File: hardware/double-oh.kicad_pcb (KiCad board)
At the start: 2 copper layers, 81.6 x 14 mm, 49 parts, among them J1 USB_B_Micro, J10 Conn_01x01, J11 Conn_01x01, J12 Conn_01x01, J13 Conn_01x01, J2 Conn_01x01, J3 Conn_01x01, J4 Conn_01x01, J5 Conn_01x01, J6 Conn_01x01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

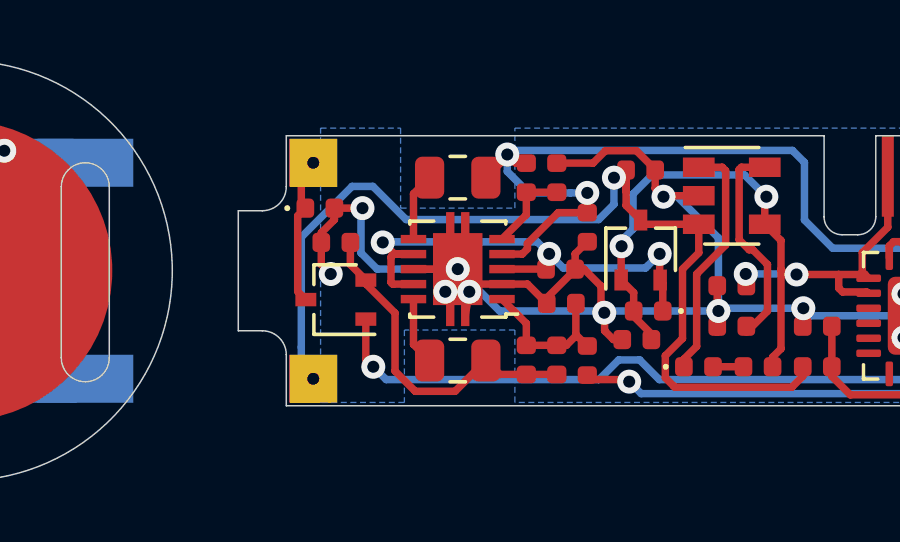
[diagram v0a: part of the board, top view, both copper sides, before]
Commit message: Rerouted for more thermal vias under buck converter
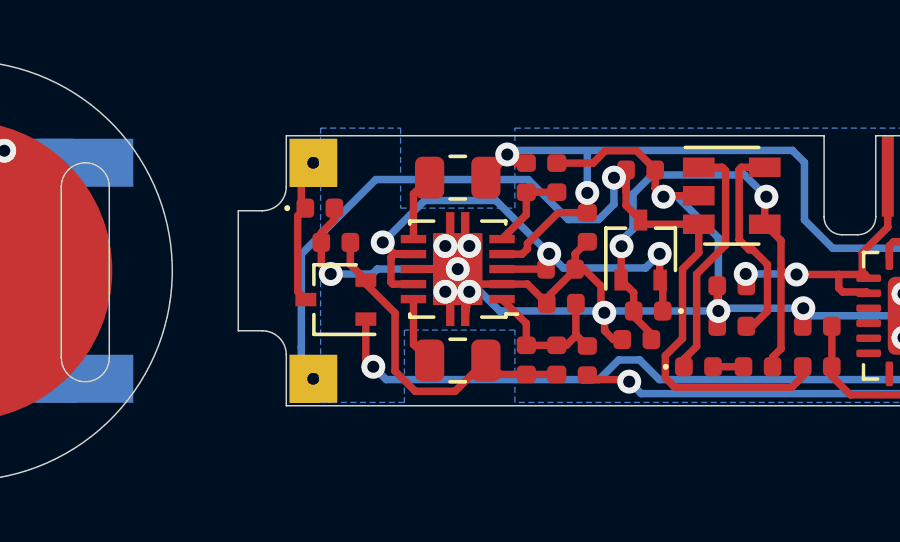
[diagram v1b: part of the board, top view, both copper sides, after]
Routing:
- net 3.3V: track 59.7 -> 57.5 mm
- net 0V: track 98.2 -> 96.6 mm, vias 25 -> 26
- net Net-(C11-Pad1): track 17.4 -> 18.5 mm

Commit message: Update DAC pin for battery level control
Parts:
- R12: value 330kΩ -> 300kΩ
- R9: value 480kΩ -> 470kΩ

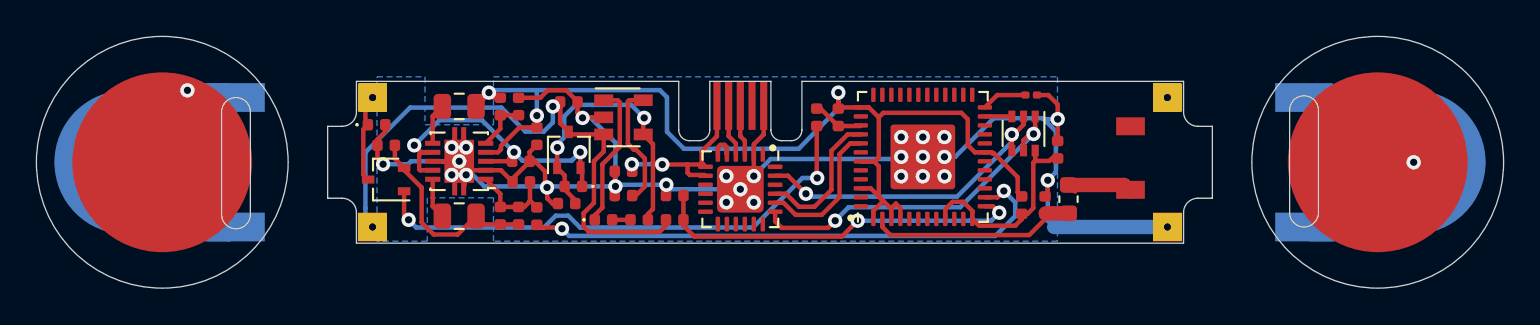
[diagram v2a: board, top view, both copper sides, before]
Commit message: Hardware update with additional safety feature
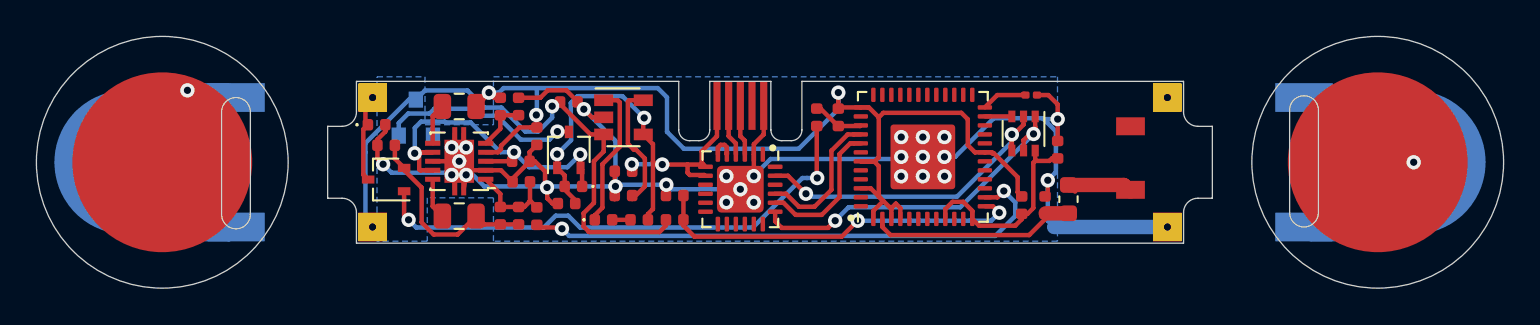
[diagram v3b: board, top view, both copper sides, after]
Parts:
- added U5: BD48KxxG, Package_TO_SOT_SMD:SOT-23, B.Cu at (103.3, 102.0)
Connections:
- Q3 pad 3: LIPO_V -> Net-(Q3-Pad3)
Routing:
- net Net-(Q3-Pad3): track 0.00 -> 11.4 mm, vias 0 -> 1
- net Net-(C11-Pad1): track 18.5 -> 19.2 mm
- net USB_VIN: track 26.8 -> 27.4 mm
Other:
- board text added: "Double-Oh v2.6 // August 2020"
- board text removed: "Double-Oh v2.5 // August 2020"

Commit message: Corrected use of voltage supervisor
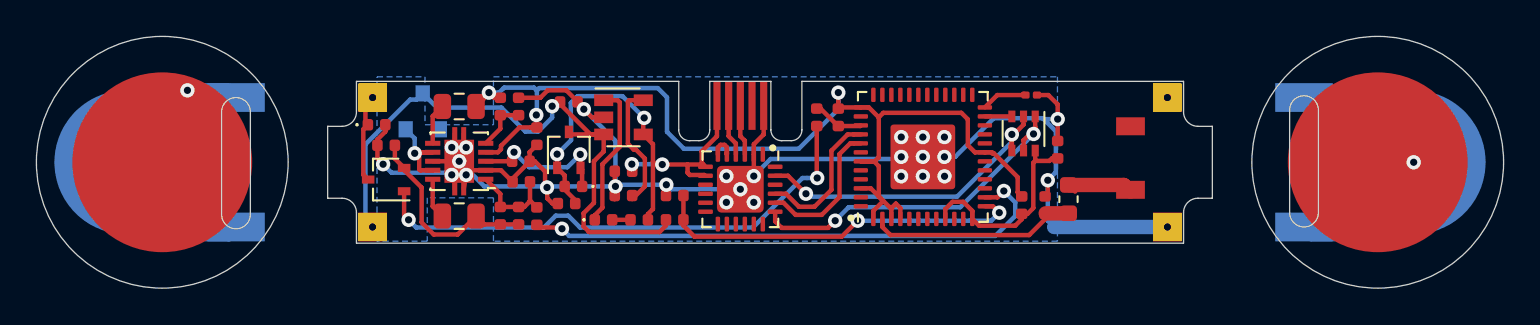
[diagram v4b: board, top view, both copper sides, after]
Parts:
- moved U5 0.52 mm to (103.7, 101.7)
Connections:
- Q3 pad 3: Net-(Q3-Pad3) -> LIPO_V
- U3 pad 7: Net-(C11-Pad1) -> TPS_EN
- U3 pad 9: Net-(C11-Pad1) -> TPS_EN
- U5 pad 2: Net-(Q3-Pad3) -> TPS_EN
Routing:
- net Net-(Q3-Pad3): track 11.4 -> 0.00 mm, vias 1 -> 0
- net Net-(C11-Pad1): track 19.2 -> 8.16 mm, vias 3 -> 2
- net TPS_EN: track 0.00 -> 5.11 mm, vias 0 -> 1
- net LIPO_V: track 32.7 -> 34.6 mm

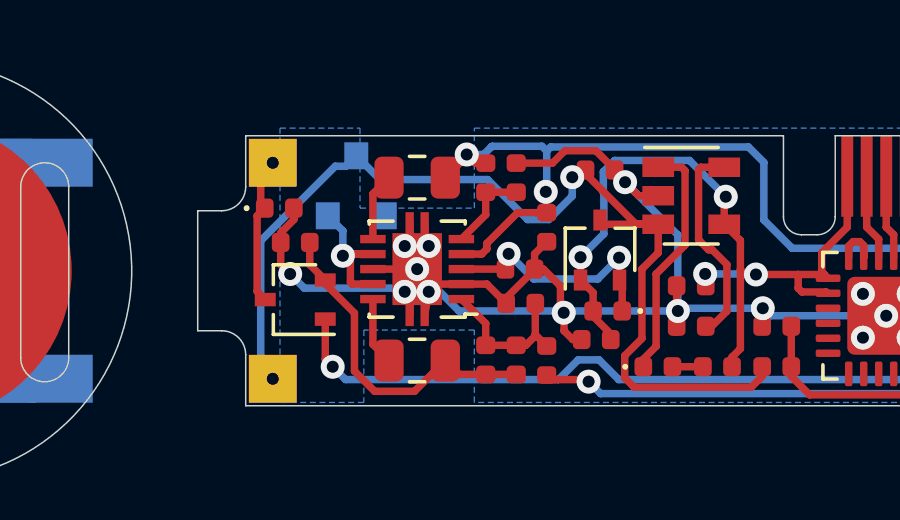
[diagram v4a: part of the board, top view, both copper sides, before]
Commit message: Added pull-up resistor for open-drain supervisor
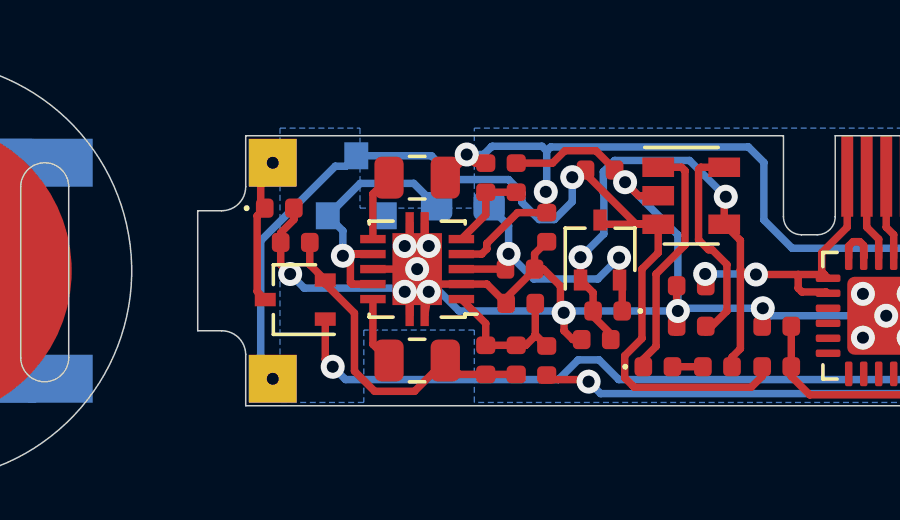
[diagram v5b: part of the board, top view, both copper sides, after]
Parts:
- added R5: 470kΩ, Resistor_SMD:R_0603_1608Metric_Pad1.05x0.95mm_HandSolder, B.Cu at (107.2, 102.3)
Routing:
- net TPS_EN: track 5.11 -> 9.50 mm
- net Net-(C11-Pad1): track 8.16 -> 10.0 mm

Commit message: Update board to v2.7
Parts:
- R5: footprint Resistor_SMD:R_0603_1608Metric_Pad1.05x0.95mm_HandSolder -> Resistor_SMD:R_0402_1005Metric; moved to F.Cu
- moved R5 4.05 mm to (103.3, 101.4), turned to 270 degrees
- moved C1 1.50 mm to (114.8, 106.5)
- moved R2 1.35 mm to (114.8, 105.0)
- moved R3 0.45 mm to (117.7, 105.9)
- moved C10 0.25 mm to (110.0, 102.8)
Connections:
- C11 pad 1: Net-(C11-Pad1) -> TPS_VIN
- D3 pad 1: Net-(C11-Pad1) -> TPS_VIN
- Q3 pad 2: Net-(C11-Pad1) -> TPS_VIN
- R5 pad 1: Net-(C11-Pad1) -> TPS_VIN
- U3 pad 3: Net-(C11-Pad1) -> TPS_VIN
- U5 pad 3: LIPO_V -> TPS_VIN
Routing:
- net TPS_VIN: track 0.00 -> 16.3 mm, vias 0 -> 3
- net Net-(C11-Pad1): track 10.0 -> 0.00 mm, vias 2 -> 0
- net Net-(R2-Pad2): track 7.07 -> 4.86 mm
- net TPS_EN: track 9.50 -> 7.33 mm
- net LIPO_V: track 34.9 -> 33.1 mm
- net USB_VIN: track 27.4 -> 26.4 mm, vias 4 -> 2
- net 0V: track 96.8 -> 97.6 mm
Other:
- board text added: "Double-Oh v2.7 // Sept. 2020"
- board text removed: "Double-Oh v2.6 // August 2020"

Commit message: Update gerbers to 2.7
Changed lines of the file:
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@@
     (thickness 0.6)
     (drawings 61)
-    (tracks 476)
+    (tracks 475)
     (zones 0)
     (modules 51)
@@
   (segment (start 116.2 106.5) (end 116.21 106.51) (width 0.25) (layer F.Cu) (net 2))
   (segment (start 116.21 107.7) (end 116.21 106.51) (width 0.25) (layer F.Cu) (net 2))
-  (segment (start 116.22 104) (end 116.21 104.01) (width 0.25) (layer F.Cu) (net 2))
   (segment (start 116.21 104.01) (end 116.21 103.21) (width 0.25) (layer F.Cu) (net 2))
   (segment (start 116.21 106.51) (end 116.21 104.01) (width 0.25) (layer F.Cu) (net 2))
-  (segment (start 118.415 104.625) (end 117.925 104.625) (width 0.25) (layer F.Cu) (net 2))
-  (segment (start 117.3 104) (end 116.22 104) (width 0.25) (layer F.Cu) (net 2))
-  (segment (start 117.925 104.625) (end 117.3 104) (width 0.25) (layer F.Cu) (net 2))
+  (segment (start 116.22 104) (end 116.21 104.01) (width 0.25) (layer F.Cu) (net 2))
+  (segment (start 118.415 104.625) (end 117.79 104) (width 0.25) (layer F.Cu) (net 2))
+  (segment (start 117.79 104) (end 116.22 104) (width 0.25) (layer F.Cu) (net 2))
   (segment (start 115.24 107.7) (end 114.224 107.7) (width 0.25) (layer F.Cu) (net 3))
   (segment (start 113.679002 107.021998) (end 113.254 107.447) (width 0.25) (layer F.Cu) (net 4))

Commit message: Add open hardware logo, switch inductor to 0806 size
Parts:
- added G***: LOGO, double-oh:OSHW_mark, B.Cu at (112.8, 103.3)
- added REF**: Fiducial_0.5mm_Mask1.5mm, Fiducial:Fiducial_0.5mm_Mask1.5mm, F.Cu at (99.5, 105.3)
- added REF**: Fiducial_0.5mm_Mask1.5mm, Fiducial:Fiducial_0.5mm_Mask1.5mm, F.Cu at (146.5, 103.6)
- L2, L3: footprint Inductor_SMD:L_0805_2012Metric -> double-oh:L_0806_2016Metric
- moved L2 0.30 mm to (105.7, 101.1)
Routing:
- net batt_out: track 11.2 -> 11.9 mm
